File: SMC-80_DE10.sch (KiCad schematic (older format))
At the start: 6 parts, among them J1 Arduino1, J2 DE10-Lite GPIO, J3 Arduino2

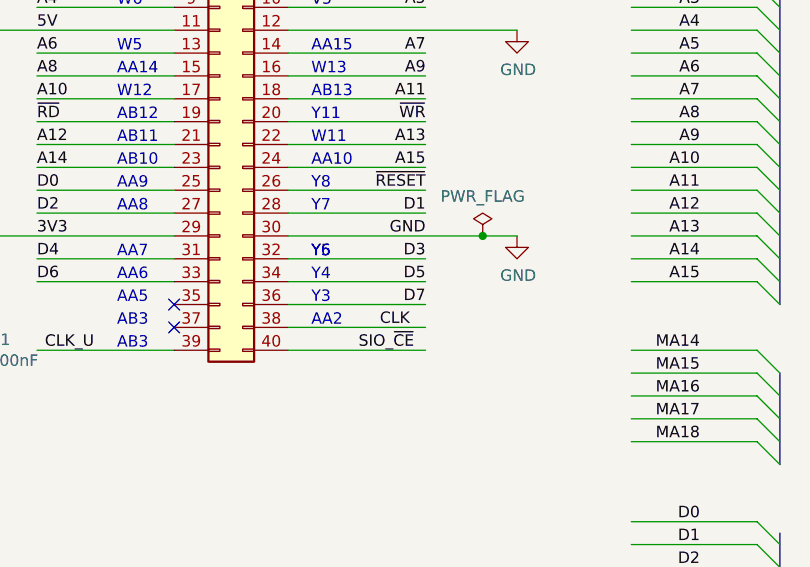
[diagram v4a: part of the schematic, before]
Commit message: removed ram/rom ce pullups
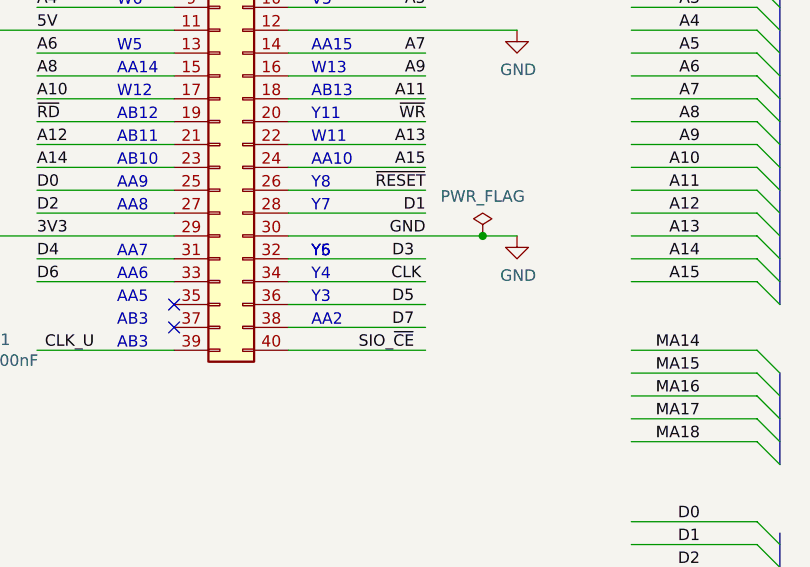
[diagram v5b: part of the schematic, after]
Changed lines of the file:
@@
 Wire Wire Line
 	3300 4000 3900 4000
-Text Label 4800 3900 0    50   ~ 0
+Text Label 4850 3700 0    50   ~ 0
 CLK
 Text Notes 3650 4000 0    50   ~ 0
@@
 Text Notes 3650 3400 0    50   ~ 0
 AA8
-Text Label 5000 3600 2    50   ~ 0
+Text Label 4950 3600 2    50   ~ 0
 D3
 Text Label 5000 3400 2    50   ~ 0
@@
 Wire Wire Line
 	4400 3400 5000 3400
-Text Label 5000 3800 2    50   ~ 0
+Text Label 4950 3900 2    50   ~ 0
 D7
-Text Label 5000 3700 2    50   ~ 0
+Text Label 4950 3800 2    50   ~ 0
 D5
 Wire Wire Line

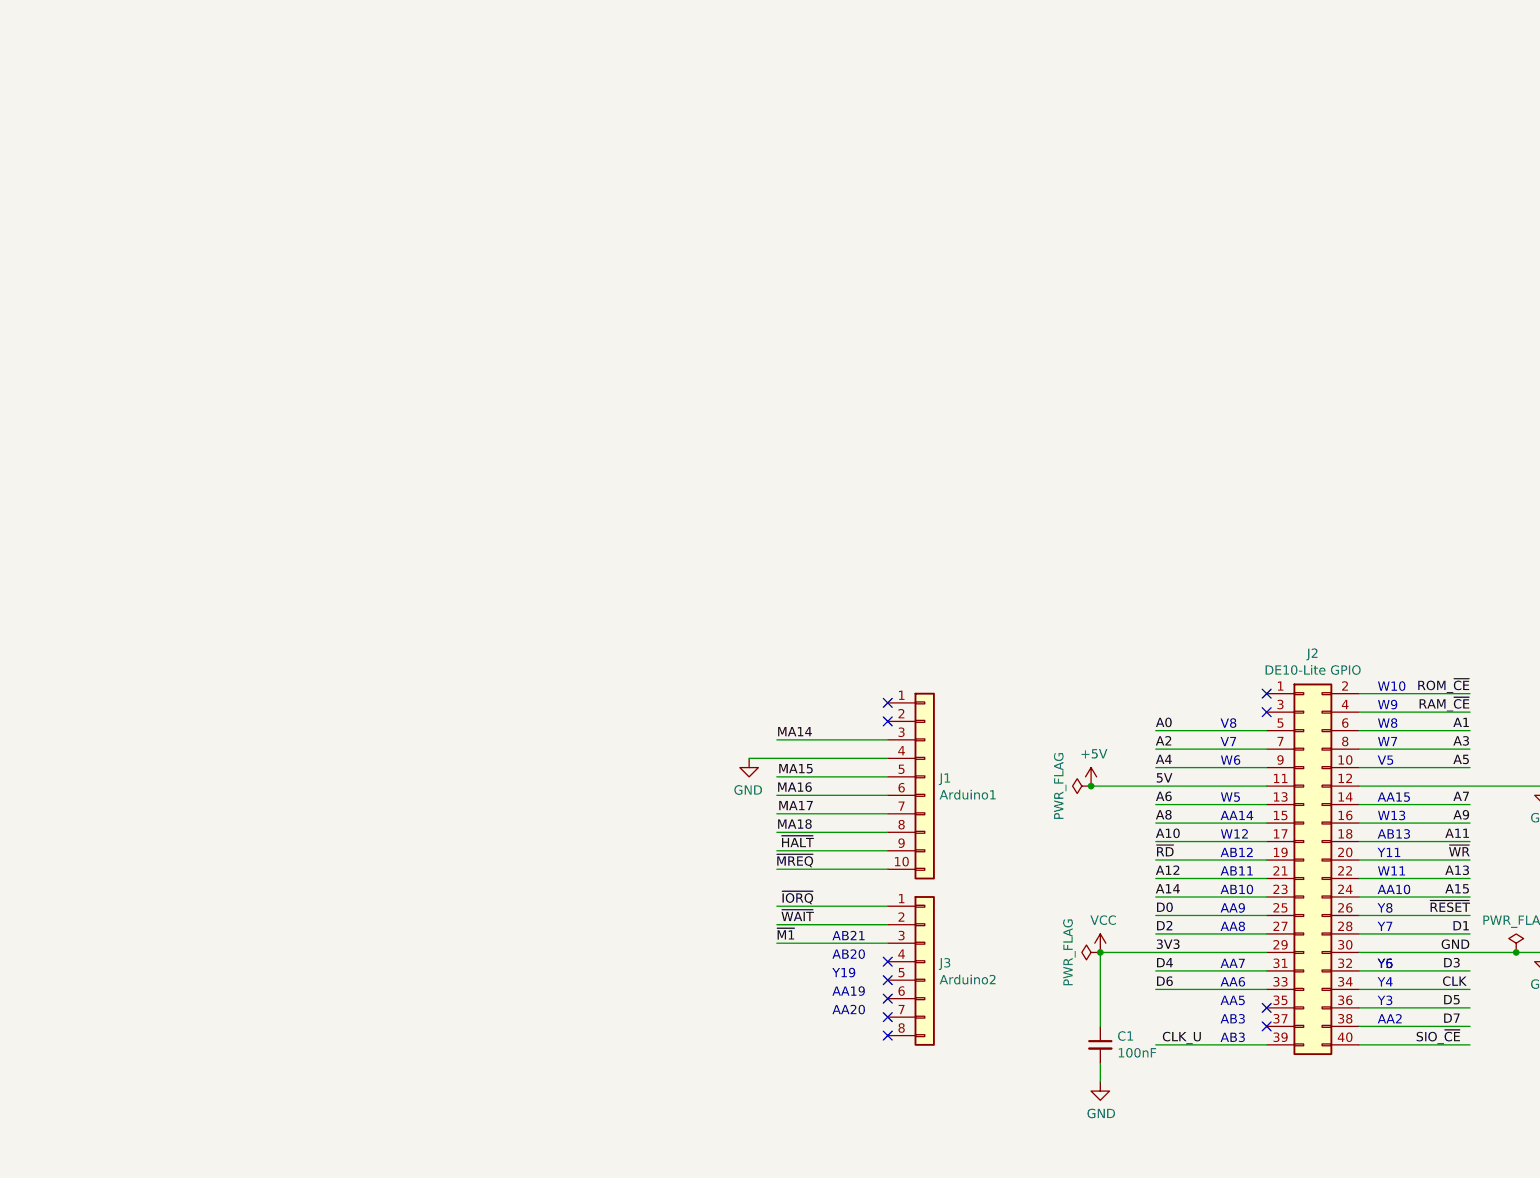
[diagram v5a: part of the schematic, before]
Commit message: added FPGA pin labels
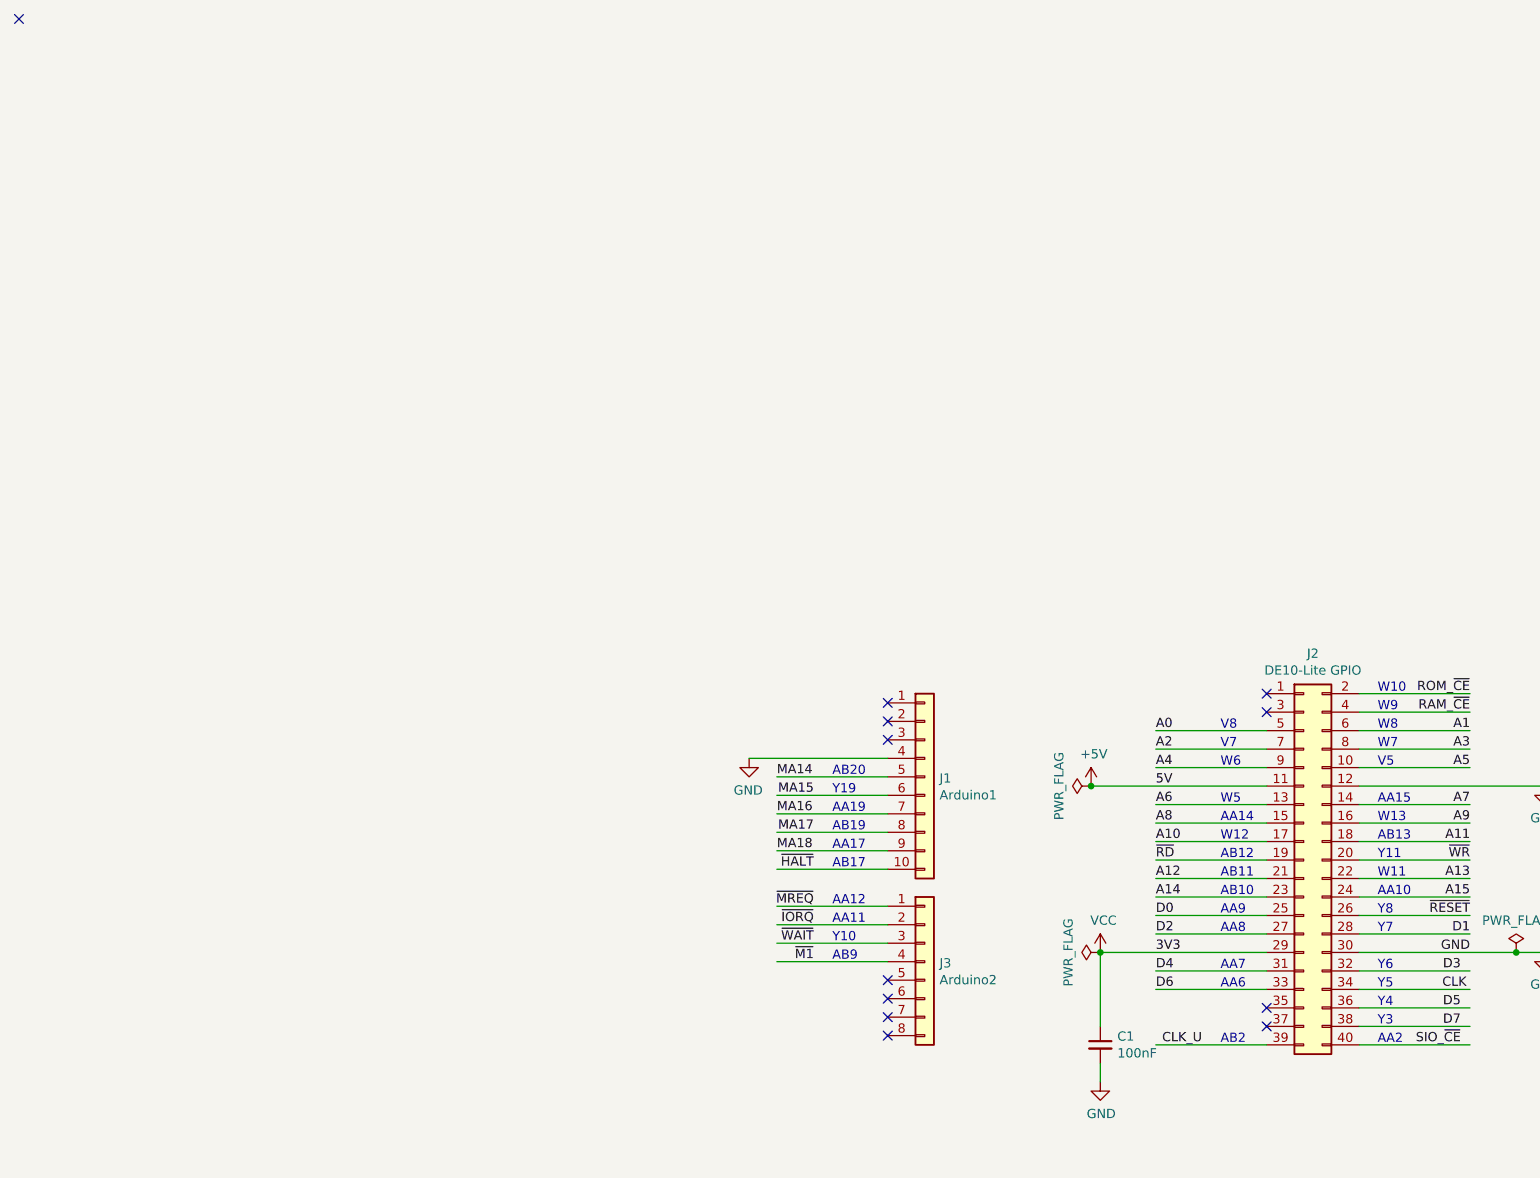
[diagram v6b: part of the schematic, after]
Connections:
- no-connect marks 12 -> 13
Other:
- note added: "AA11"
- note added: "AA12"
- note added: "AA17"
- note added: "AB17"
- note added: "AB19"
- note added: "AB2"
- note added: "AB9"
- note added: "Y10"
- note removed: "AA20"
- note removed: "AA5"
- note removed: "AB21"
- note removed: "AB3"
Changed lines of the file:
@@
 Wire Wire Line
 	3350 5800 3350 5900
-Text Label 1350 3450 2    50   ~ 0
+Text Label 1450 3550 2    50   ~ 0
 ~M1
-Text Label 1450 3250 2    50   ~ 0
+Text Label 1450 3350 2    50   ~ 0
 ~IORQ
-Text Notes 1550 3850 0    50   ~ 0
-AA20
-Text Notes 1550 3450 0    50   ~ 0
-AB21
-Text Notes 1550 3750 0    50   ~ 0
+Text Notes 1550 3550 0    50   ~ 0
+AB9
+Text Notes 1550 2750 0    50   ~ 0
 AA19
-Text Notes 1550 3650 0    50   ~ 0
+Text Notes 1550 2650 0    50   ~ 0
 Y19
-Text Notes 1550 3550 0    50   ~ 0
+Text Notes 1550 2550 0    50   ~ 0
 AB20
 $Comp
@@
 $EndComp
 Wire Wire Line
-	1850 2950 1250 2950
+	1850 3050 1250 3050
+Wire Wire Line
+	1850 3550 1250 3550
+Wire Wire Line
+	1850 3250 1250 3250
+Wire Wire Line
+	1850 3350 1250 3350
 Wire Wire Line
 	1850 3450 1250 3450
-Wire Wire Line
-	1850 3050 1250 3050
-Wire Wire Line
-	1850 3250 1250 3250
-Wire Wire Line
-	1850 3350 1250 3350
 Wire Wire Line
 	1100 2450 1850 2450
@@
 CLK
 Text Notes 3650 4000 0    50   ~ 0
-AB3
+AB2
 Wire Wire Line
 	3300 3300 3900 3300
@@
 Text Label 3300 3200 0    50   ~ 0
 A14
-Text Label 1250 2650 0    50   ~ 0
+Text Label 1250 2750 0    50   ~ 0
 MA16
-Text Label 1250 2850 0    50   ~ 0
+Text Label 1250 2950 0    50   ~ 0
 MA18
 Text Label 3300 3100 0    50   ~ 0
 A12
 Wire Wire Line
-	1850 2850 1250 2850
-Wire Wire Line
-	1250 2650 1850 2650
+	1850 2950 1250 2950
+Wire Wire Line
+	1250 2750 1850 2750
 Text Notes 3650 3600 0    50   ~ 0
 AA7
 Text Notes 3650 3700 0    50   ~ 0
 AA6
-Text Notes 3650 3800 0    50   ~ 0
-AA5
-Text Notes 3650 3900 0    50   ~ 0
-AB3
 Wire Wire Line
 	5000 3100 4400 3100
@@
 	5000 3200 4400 3200
 Wire Wire Line
-	1850 2750 1250 2750
+	1850 2850 1250 2850
 Text Label 5000 3100 2    50   ~ 0
 A13
 Text Label 5000 3200 2    50   ~ 0
 A15
-Text Label 1450 2750 2    50   ~ 0
+Text Label 1450 2850 2    50   ~ 0
 MA17
 Text Notes 4500 3600 0    50   ~ 0
 Y6
-Text Notes 4500 3600 0    50   ~ 0
+Text Notes 4500 3700 0    50   ~ 0
 Y5
-Text Notes 4500 3700 0    50   ~ 0
+Text Notes 4500 3800 0    50   ~ 0
 Y4
 Wire Wire Line
@@
 Text Notes 3650 2900 0    50   ~ 0
 W12
+Text Notes 4500 4000 0    50   ~ 0
+AA2
 Text Notes 4500 3900 0    50   ~ 0
-AA2
-Text Notes 4500 3800 0    50   ~ 0
 Y3
 Text Notes 4500 3000 0    50   ~ 0
@@
 Wire Wire Line
 	5000 2200 4400 2200
+Text Label 1450 3250 2    50   ~ 0
+~MREQ
 Text Label 1450 3050 2    50   ~ 0
-~MREQ
-Text Label 1450 2950 2    50   ~ 0
 ~HALT
-Text Label 1450 3350 2    50   ~ 0
+Text Label 1450 3450 2    50   ~ 0
 ~WAIT
 $Sheet
@@
 	1    0    0    -1
 $EndComp
-NoConn ~ 1850 3550
 NoConn ~ 1850 3650
 NoConn ~ 1850 3750
@@
 NoConn ~ 3900 3900
 NoConn ~ 3900 3800
-Text Label 1250 2350 0    50   ~ 0
+Text Label 1250 2550 0    50   ~ 0
 MA14
 Wire Wire Line
-	1250 2350 1850 2350
-Wire Wire Line
-	1850 2550 1250 2550
-Text Label 1450 2550 2    50   ~ 0
+	1250 2550 1850 2550
+Wire Wire Line
+	1850 2650 1250 2650
+Text Label 1450 2650 2    50   ~ 0
 MA15
 Wire Bus Line
@@
 Entry Wire Line
 	6450 4400 6550 4500
+Text Notes 1550 3250 0    50   ~ 0
+AA12
+Text Notes 1550 3350 0    50   ~ 0
+AA11
+Text Notes 1550 3450 0    50   ~ 0
+Y10
+NoConn ~ 1850 2350
+NoConn ~ -2850 -1550
+Text Notes 1550 2850 0    50   ~ 0
+AB19
+Text Notes 1550 2950 0    50   ~ 0
+AA17
+Text Notes 1550 3050 0    50   ~ 0
+AB17
 Wire Bus Line
 	6550 4100 6550 4500

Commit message: final version 1.0
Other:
- note removed: "Y3"
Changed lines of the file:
@@
 	3300 3300 3900 3300
 Wire Wire Line
-	3300 3400 3900 3400
-Wire Wire Line
-	3300 3600 3900 3600
-Wire Wire Line
-	3300 3700 3900 3700
-Text Label 3300 3400 0    50   ~ 0
+	5000 3400 4400 3400
+Wire Wire Line
+	5000 3600 4400 3600
+Wire Wire Line
+	5000 3800 4400 3800
+Text Label 5000 3400 2    50   ~ 0
 D2
-Text Label 3300 3600 0    50   ~ 0
+Text Label 5000 3600 2    50   ~ 0
 D4
-Text Label 3300 3700 0    50   ~ 0
+Text Label 5000 3800 2    50   ~ 0
 D6
 Text Label 3300 3000 0    50   ~ 0
@@
 Wire Wire Line
 	3900 3000 3300 3000
-Text Label 3300 3300 0    50   ~ 0
+Text Label 4900 3300 0    50   ~ 0
 D0
 Text Notes 3650 3000 0    50   ~ 0
@@
 Text Notes 3650 3400 0    50   ~ 0
 AA8
-Text Label 4950 3600 2    50   ~ 0
+Text Label 3300 3600 0    50   ~ 0
 D3
-Text Label 5000 3400 2    50   ~ 0
+Text Label 3300 3400 0    50   ~ 0
 D1
 Wire Wire Line
-	4400 3600 5000 3600
-Wire Wire Line
-	4400 3400 5000 3400
-Text Label 4950 3900 2    50   ~ 0
+	3900 3600 3300 3600
+Wire Wire Line
+	3900 3400 3300 3400
+Text Label 3300 3800 0    50   ~ 0
 D7
-Text Label 4950 3800 2    50   ~ 0
+Text Label 3300 3700 0    50   ~ 0
 D5
 Wire Wire Line
-	4400 3800 5000 3800
+	3900 3700 3300 3700
 Wire Wire Line
 	4400 3700 5000 3700
@@
 Text Notes 4500 3300 0    50   ~ 0
 Y8
-Text Notes 4500 3400 0    50   ~ 0
+Text Notes 4600 3400 2    50   ~ 0
 Y7
 Wire Wire Line
-	3900 3100 3300 3100
-Wire Wire Line
-	3900 3200 3300 3200
-Text Label 3300 3200 0    50   ~ 0
+	4400 3100 5000 3100
+Wire Wire Line
+	4400 3200 5000 3200
+Text Label 5000 3200 2    50   ~ 0
 A14
 Text Label 1250 2750 0    50   ~ 0
@@
 Text Label 1250 2950 0    50   ~ 0
 MA18
-Text Label 3300 3100 0    50   ~ 0
+Text Label 5000 3100 2    50   ~ 0
 A12
 Wire Wire Line
@@
 AA6
 Wire Wire Line
-	5000 3100 4400 3100
-Wire Wire Line
-	5000 3200 4400 3200
+	3300 3100 3900 3100
+Wire Wire Line
+	3300 3200 3900 3200
 Wire Wire Line
 	1850 2850 1250 2850
-Text Label 5000 3100 2    50   ~ 0
+Text Label 3300 3100 0    50   ~ 0
 A13
-Text Label 5000 3200 2    50   ~ 0
+Text Label 3300 3200 0    50   ~ 0
 A15
 Text Label 1450 2850 2    50   ~ 0
@@
 Text Notes 4500 4000 0    50   ~ 0
 AA2
-Text Notes 4500 3900 0    50   ~ 0
-Y3
 Text Notes 4500 3000 0    50   ~ 0
 Y11
@@
 Connection ~ 3000 3500
 Wire Wire Line
-	5000 2700 4400 2700
+	3300 2700 3900 2700
 $Comp
 L Device:C_Small C1
@@
 	5250 3500 4400 3500
 Wire Wire Line
-	4400 2400 5000 2400
+	3900 2400 3300 2400
 Wire Wire Line
 	5000 3000 4400 3000
 Connection ~ 5250 3500
 Wire Wire Line
-	5000 2900 4400 2900
-Text Label 5000 2800 2    50   ~ 0
+	3300 2900 3900 2900
+Text Label 3300 2800 0    50   ~ 0
 A9
-Text Label 5000 2900 2    50   ~ 0
+Text Label 3300 2900 0    50   ~ 0
 A11
 Wire Wire Line
-	5000 2800 4400 2800
+	3300 2800 3900 2800
 Text Label 5000 3000 2    50   ~ 0
 ~WR
 Wire Wire Line
-	3900 2700 3300 2700
-Text Label 3300 2800 0    50   ~ 0
+	4400 2700 5000 2700
+Text Label 5000 2800 2    50   ~ 0
 A8
-Text Label 3300 2900 0    50   ~ 0
+Text Label 5000 2900 2    50   ~ 0
 A10
 Wire Wire Line
-	3900 2800 3300 2800
-Text Label 5000 3300 2    50   ~ 0
+	4400 2800 5000 2800
+Text Label 3550 3300 2    50   ~ 0
 ~RESET
 Wire Wire Line
-	3900 2900 3300 2900
+	4400 2900 5000 2900
 Text Label 5000 2200 2    50   ~ 0
 RAM_~CE
@@
 	1    0    0    -1
 $EndComp
+Text Label 3300 2700 0    50   ~ 0
+A7
 Text Label 5000 2700 2    50   ~ 0
-A7
-Text Label 3300 2700 0    50   ~ 0
 A6
+Text Label 3300 2500 0    50   ~ 0
+A5
 Text Label 5000 2500 2    50   ~ 0
-A5
-Text Label 3300 2500 0    50   ~ 0
 A4
+Text Label 3300 2400 0    50   ~ 0
+A3
 Text Label 5000 2400 2    50   ~ 0
-A3
-Text Label 3300 2400 0    50   ~ 0
 A2
+Text Label 3300 2300 0    50   ~ 0
+A1
 Text Label 5000 2300 2    50   ~ 0
-A1
-Text Label 3300 2300 0    50   ~ 0
 A0
 $Comp
@@
 	5400 2600 4400 2600
 Wire Wire Line
-	5000 2500 4400 2500
-Wire Wire Line
-	5000 2300 4400 2300
-Wire Wire Line
-	3900 2500 3300 2500
-Wire Wire Line
-	3900 2400 3300 2400
-Wire Wire Line
-	3900 2300 3300 2300
+	3300 2500 3900 2500
+Wire Wire Line
+	3300 2300 3900 2300
+Wire Wire Line
+	4400 2500 5000 2500
+Wire Wire Line
+	4400 2400 5000 2400
+Wire Wire Line
+	4400 2300 5000 2300
 Wire Wire Line
 	5000 2200 4400 2200
@@
 CLK_U
 Wire Wire Line
-	4400 3900 5000 3900
+	3900 3800 3300 3800
 Text Label 7450 2900 2    50   ~ 0
 CLK_U
@@
 NoConn ~ 1850 3950
 NoConn ~ 3900 3900
-NoConn ~ 3900 3800
 Text Label 1250 2550 0    50   ~ 0
 MA14
@@
 Text Notes 1550 3050 0    50   ~ 0
 AB17
+NoConn ~ 4400 3900
 Wire Bus Line
 	6550 4100 6550 4500

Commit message: reorganized SIO
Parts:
- renumbered J3 to J2, J2 to J3
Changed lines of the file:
@@
 $EndDescr
 $Comp
-L power:VCC #PWR07
+L power:VCC #PWR02
 U 1 1 5E6DA593
 P 2850 5450
-F 0 "#PWR07" H 2850 5300 50  0001 C CNN
+F 0 "#PWR02" H 2850 5300 50  0001 C CNN
 F 1 "VCC" H 2867 5623 50  0000 C CNN
 F 2 "" H 2850 5450 50  0001 C CNN
@@
 $EndComp
 $Comp
-L power:GND #PWR08
+L power:GND #PWR06
 U 1 1 5E75C5FC
 P 3350 5900
-F 0 "#PWR08" H 3350 5650 50  0001 C CNN
+F 0 "#PWR06" H 3350 5650 50  0001 C CNN
 F 1 "GND" H 3355 5727 50  0000 C CNN
 F 2 "" H 3350 5900 50  0001 C CNN
@@
 	3000 4200 3000 4100
 $Comp
-L power:GND #PWR06
+L power:GND #PWR05
 U 1 1 5DA1CD65
 P 3000 4200
-F 0 "#PWR06" H 3000 3950 50  0001 C CNN
+F 0 "#PWR05" H 3000 3950 50  0001 C CNN
 F 1 "GND" H 3005 4027 50  0000 C CNN
 F 2 "" H 3000 4200 50  0001 C CNN
@@
 Connection ~ 2950 2600
 $Comp
-L power:+5V #PWR02
+L power:+5V #PWR03
 U 1 1 5DA0C153
 P 2950 2600
-F 0 "#PWR02" H 2950 2450 50  0001 C CNN
+F 0 "#PWR03" H 2950 2450 50  0001 C CNN
 F 1 "+5V" H 2965 2773 50  0000 C CNN
 F 2 "" H 2950 2600 50  0001 C CNN
@@
 NoConn ~ 3900 2100
 $Comp
-L Connector_Generic:Conn_02x20_Odd_Even J2
+L Connector_Generic:Conn_02x20_Odd_Even J3
 U 1 1 5D754F95
 P 4100 3000
-F 0 "J2" H 4150 4117 50  0000 C CNN
+F 0 "J3" H 4150 4117 50  0000 C CNN
 F 1 "DE10-Lite GPIO" H 4150 4026 50  0000 C CNN
 F 2 "Connector_PinSocket_2.54mm:PinSocket_2x20_P2.54mm_Vertical" H 4100 3000 50  0001 C CNN
@@
 A0
 $Comp
-L power:GND #PWR05
+L power:GND #PWR08
 U 1 1 5D763690
 P 5400 3500
-F 0 "#PWR05" H 5400 3250 50  0001 C CNN
+F 0 "#PWR08" H 5400 3250 50  0001 C CNN
 F 1 "GND" H 5405 3327 50  0000 C CNN
 F 2 "" H 5400 3500 50  0001 C CNN
@@
 $EndComp
 $Comp
-L power:GND #PWR03
+L power:GND #PWR07
 U 1 1 5D762CD7
 P 5400 2600
-F 0 "#PWR03" H 5400 2350 50  0001 C CNN
+F 0 "#PWR07" H 5400 2350 50  0001 C CNN
 F 1 "GND" H 5405 2427 50  0000 C CNN
 F 2 "" H 5400 2600 50  0001 C CNN
@@
 NoConn ~ 1850 2150
 $Comp
-L Connector_Generic:Conn_01x08 J3
+L Connector_Generic:Conn_01x08 J2
 U 1 1 5DB3A357
 P 2050 3550
-F 0 "J3" H 2130 3542 50  0000 L CNN
+F 0 "J2" H 2130 3542 50  0000 L CNN
 F 1 "Arduino2" H 2130 3451 50  0000 L CNN
 F 2 "Connector_PinHeader_2.54mm:PinHeader_1x08_P2.54mm_Vertical" H 2050 3550 50  0001 C CNN
